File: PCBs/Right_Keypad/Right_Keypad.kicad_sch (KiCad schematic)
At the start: 33 parts, among them J1 Conn_Right_Keypad, SW1 SW_Push, SW10 SW_Push, SW11 SW_Push, SW12 SW_Push, SW13 SW_Push, SW14 SW_Push, SW15 SW_Push, SW16 SW_Push, SW17 SW_Push, SW18 SW_Push, SW19 SW_Push, SW2 SW_Push, SW20 SW_Push, SW21 SW_Push, SW22 SW_Push, SW3 SW_Push, SW4 SW_Push, SW5 SW_Push, SW6 SW_Push, SW7 SW_Push, SW8 SW_Push, SW9 SW_Push, U1 74HC165, U2 74HC165, U3 74HC165

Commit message: wip
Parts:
- C1, C2, C3: footprint (none) -> Capacitor_THT:C_Disc_D5.0mm_W2.5mm_P2.50mm
- J1: footprint (none) -> Connector_IDC:IDC-Header_2x05_P2.54mm_Vertical
- R1: footprint (none) -> Resistor_THT:R_Axial_DIN0207_L6.3mm_D2.5mm_P7.62mm_Horizontal
- SW1, SW10, SW11, SW12, SW13, SW14, SW15, SW16, SW17, SW18, SW19, SW2, SW20, SW21, SW22, SW3, SW4, SW5, SW6, SW7, SW8, SW9: footprint (none) -> Custom_Footprints:SW_PUSH-12mm_Grid
- U1, U2, U3: footprint (none) -> Package_DIP:DIP-16_W7.62mm
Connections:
- net +5V: now also C2.2, C3.2, U2.16 (VCC), U3.16 (VCC)
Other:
- moved on the sheet: C1

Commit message: before moving keypad shift regs
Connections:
- net at RN3.2 (R1): now also U3.3 (D4); no longer U3.6 (D7)
- net at RN3.3 (R2): now also U3.14 (D3); no longer U3.5 (D6)
- net at RN3.4 (R3), U3.4 (D5): now also SW14.2; no longer SW22.2
- net at RN3.9 (R8), U3.11 (D0): now also SW22.2; no longer SW17.2
- net at RN1.3 (R2), SW7.2: now also U1.14 (D3); no longer U1.5 (D6)
- net at SW8.2, U1.6 (D7): now also RN1.8 (R7); no longer RN1.2 (R1)
- net at RN1.9 (R8), U1.11 (D0): now also SW3.2; no longer SW1.2
- net at RN1.4 (R3), U1.4 (D5): now also SW4.2; no longer SW6.2
- net at RN2.9 (R8), U2.11 (D0): now also SW19.2; no longer SW9.2
- net at RN2.4 (R3), U2.4 (D5): now also SW11.2; no longer SW14.2
- new net: RN3.5 (R4), SW15.2, U3.13 (D2)
- new net: RN3.6 (R5), SW16.2, U3.5 (D6)
- new net: RN3.7 (R6), SW20.2, U3.12 (D1)
- new net: RN3.8 (R7), SW21.2, U3.6 (D7)
- new net: RN1.6 (R5), SW2.2, U1.5 (D6)
- new net: RN1.5 (R4), SW1.2, U1.13 (D2)
- new net: RN1.7 (R6), SW5.2, U1.12 (D1)
- new net: RN1.2 (R1), SW10.2, U1.3 (D4)
- new net: RN2.3 (R2), SW6.2, U2.14 (D3)
- new net: RN2.8 (R7), SW18.2, U2.6 (D7)
- new net: RN2.2 (R1), SW9.2, U2.3 (D4)
- new net: RN2.7 (R6), SW17.2, U2.12 (D1)
- new net: RN2.5 (R4), SW12.2, U2.13 (D2)
- new net: RN2.6 (R5), SW13.2, U2.5 (D6)
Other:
- moved on the sheet: SW1, SW10, SW11, SW12, SW13, SW14, SW15, SW16, SW17, SW18, SW19, SW2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

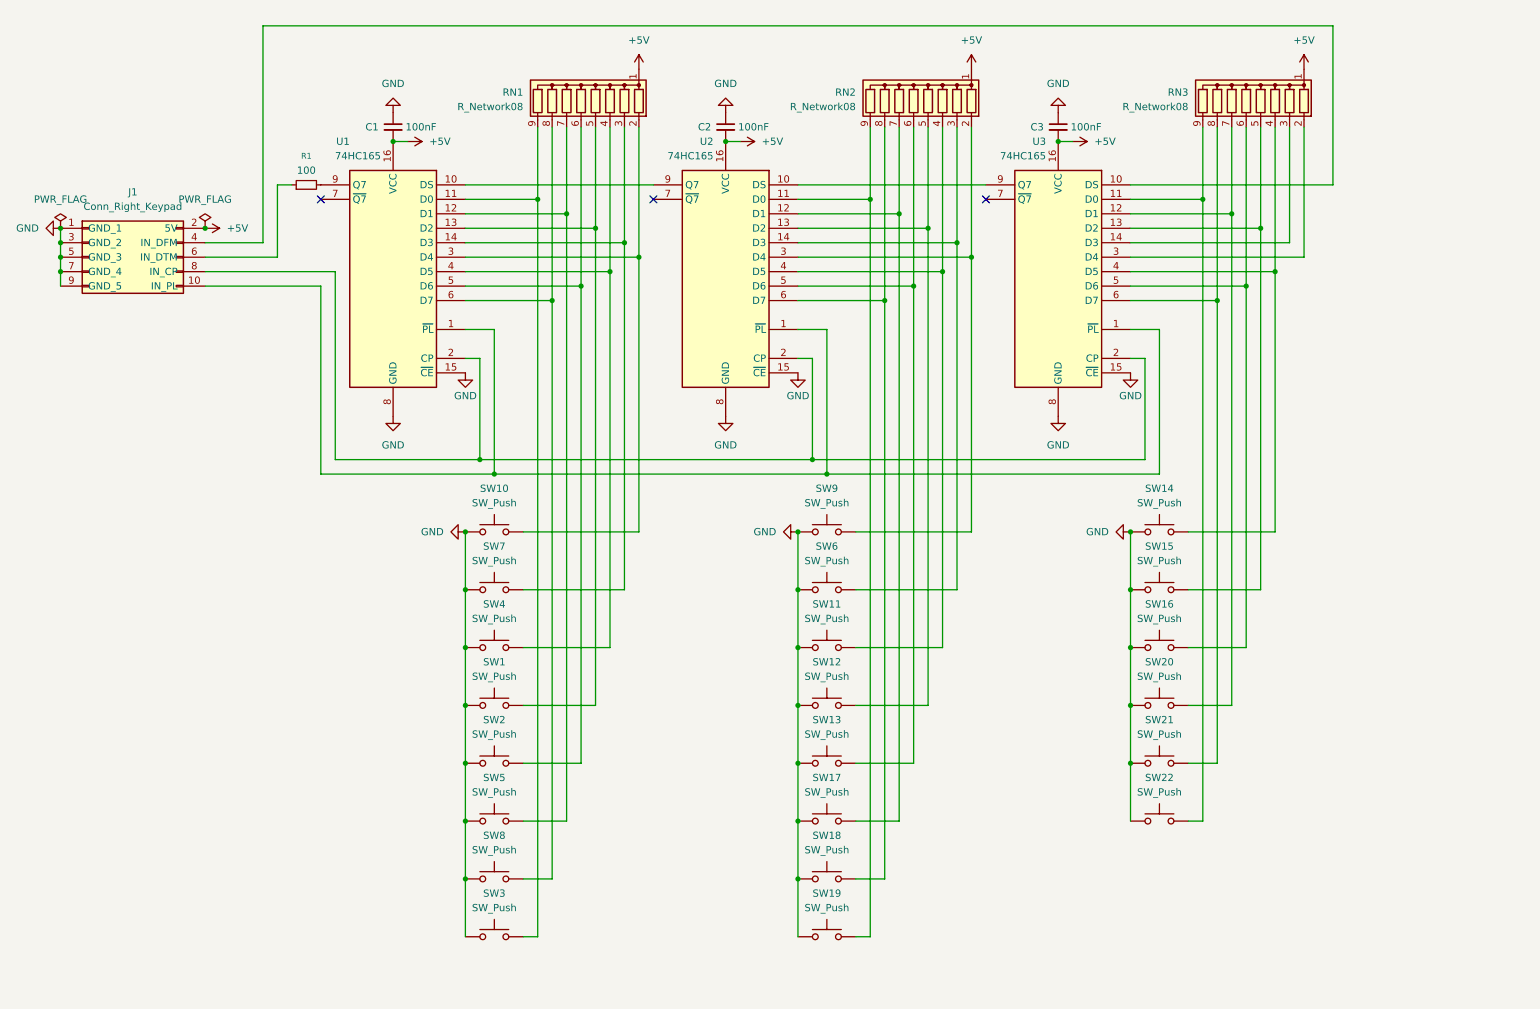
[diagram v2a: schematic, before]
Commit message: Moved shift registers
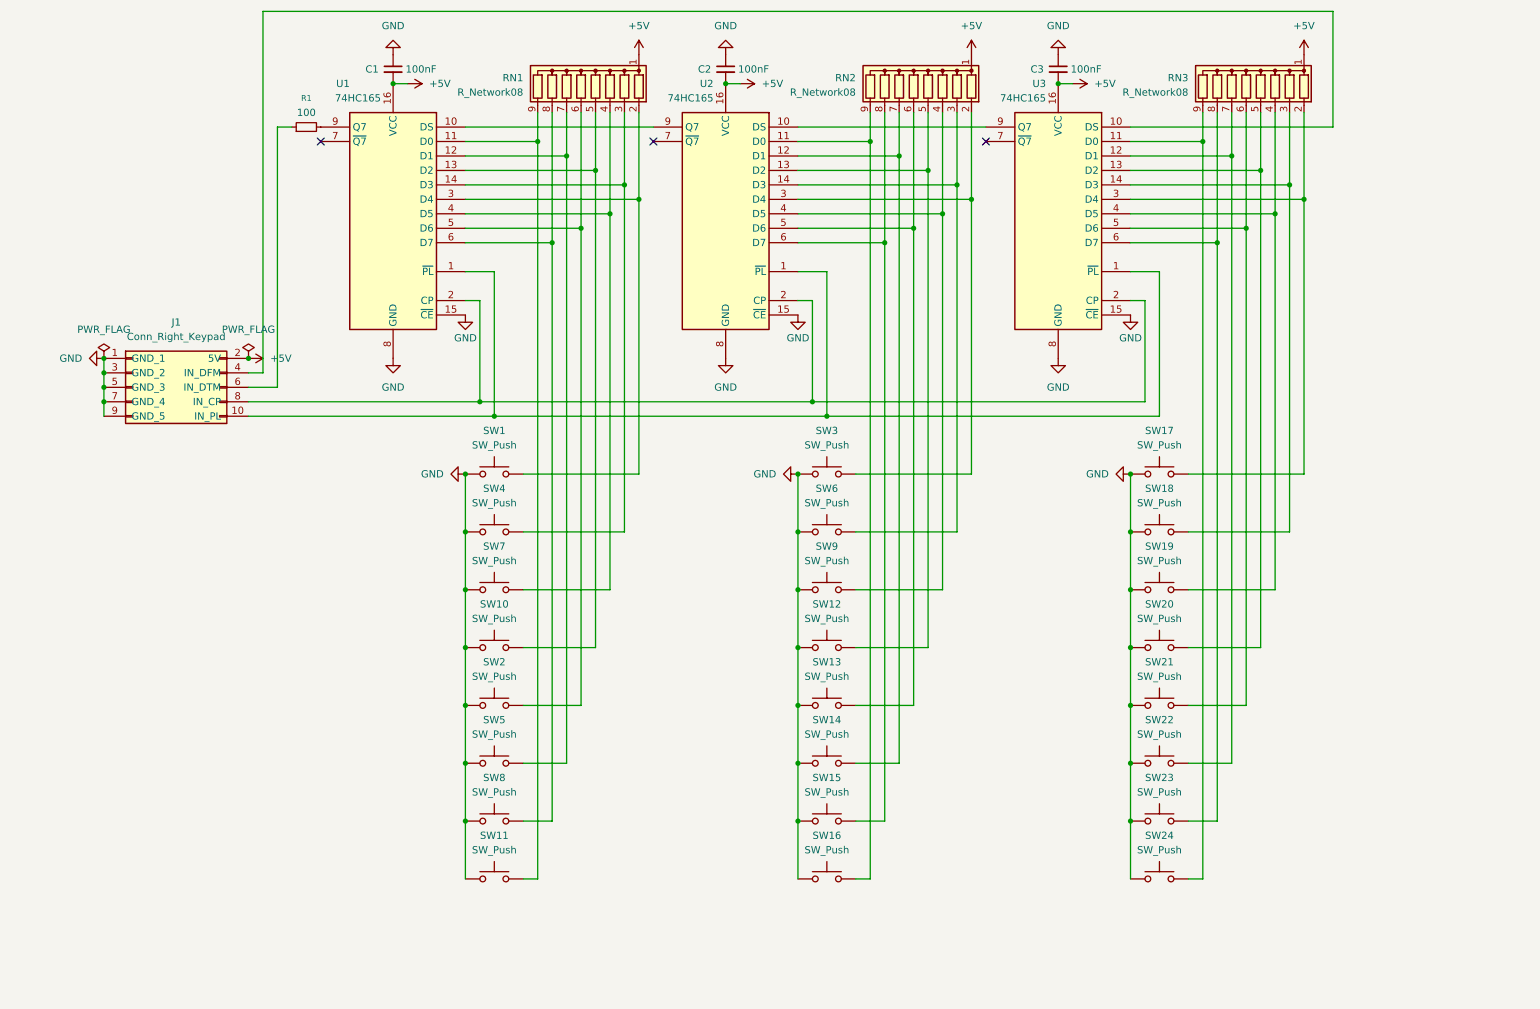
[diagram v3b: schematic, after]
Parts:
- added SW23, SW24: SW_Push, Custom_Footprints:SW_PUSH-12mm_Grid, symbol Switch:SW_Push
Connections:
- net GND: now also SW23.1, SW24.1
- net at RN3.5 (R4), U3.13 (D2): now also SW20.2; no longer SW15.2
- net at RN3.2 (R1), U3.3 (D4): now also SW17.2
- net at RN3.3 (R2), U3.14 (D3): now also SW18.2
- net at RN3.4 (R3), U3.4 (D5): now also SW19.2; no longer SW14.2
- net at RN3.6 (R5), U3.5 (D6): now also SW21.2; no longer SW16.2
- net at RN3.7 (R6), U3.12 (D1): now also SW22.2; no longer SW20.2
- net at RN3.8 (R7), U3.6 (D7): now also SW23.2; no longer SW21.2
- net at RN3.9 (R8), U3.11 (D0): now also SW24.2; no longer SW22.2
- net at RN2.4 (R3), U2.4 (D5): now also SW9.2; no longer SW11.2
- net at RN1.3 (R2), U1.14 (D3): now also SW4.2; no longer SW7.2
- net at RN1.9 (R8), U1.11 (D0): now also SW11.2; no longer SW3.2
- net at RN1.4 (R3), U1.4 (D5): now also SW7.2; no longer SW4.2
- net at RN1.5 (R4), U1.13 (D2): now also SW10.2; no longer SW1.2
- net at RN1.2 (R1), U1.3 (D4): now also SW1.2; no longer SW10.2
- net at RN2.8 (R7), U2.6 (D7): now also SW15.2; no longer SW18.2
- net at RN2.2 (R1), U2.3 (D4): now also SW3.2; no longer SW9.2
- net at RN2.7 (R6), U2.12 (D1): now also SW14.2; no longer SW17.2
- net at RN2.9 (R8), U2.11 (D0): now also SW16.2; no longer SW19.2
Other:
- moved on the sheet: C1, C2, C3, J1, R1, RN1, RN2, RN3, SW1, SW10, SW11, SW12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

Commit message: before UART+RS485
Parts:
- removed C2, C3: 100nF, Capacitor_THT:C_Disc_D5.0mm_W2.5mm_P2.50mm, symbol Device:C_Small
- removed RN2, RN3: R_Network08, Resistor_THT:R_Array_SIP9, symbol Device:R_Network08
- removed U2, U3: 74HC165, Package_DIP:DIP-16_W7.62mm, symbol 74xx:74HC165
- added D1, D10, D11, D12, D13, D14, D15, D16, D17, D18, D19, D2, D20, D21, D22, D23, D24, D3, D4, D5, D6, D7, D8, D9: D, Diode_SMD:D_SOD-123, symbol Device:D
- added Q1, Q2, Q3: NPN, Package_TO_SOT_THT:TO-92_Inline, symbol Simulation_SPICE:NPN
- added R2, R3, R4: 10k, Resistor_THT:R_Axial_DIN0207_L6.3mm_D2.5mm_P7.62mm_Horizontal, symbol Device:R_Small
- J1: footprint Connector_IDC:IDC-Header_2x05_P2.54mm_Vertical -> Connector_IDC:IDC-Header_2x08_P2.54mm_Vertical
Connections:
- net GND: now also J1.11 (GND_6), J1.13 (GND_7), J1.15 (GND_8), Q1.3 (E), Q2.3 (E), Q3.3 (E); no longer SW1.1, SW10.1, SW11.1, SW12.1, SW13.1, SW14.1, SW15.1, SW16.1, SW17.1, SW18.1, SW19.1, SW2.1, SW20.1, SW21.1, SW22.1, SW23.1, SW24.1, SW3.1, SW4.1, SW5.1, SW6.1, SW7.1, SW8.1, SW9.1
- net at SW15.2: now also D15.1 (K)
- net at SW17.2: now also D17.1 (K)
- net at SW18.2: now also D18.1 (K)
- net at SW19.2: now also D19.1 (K)
- net at SW20.2: now also D20.1 (K)
- net at SW21.2: now also D21.1 (K)
- net at SW22.2: now also D22.1 (K)
- net at SW23.2: now also D23.1 (K)
- net at SW24.2: now also D24.1 (K)
- net at RN1.9 (R8), U1.11 (D0): now also D1.2 (A), D17.2 (A), D9.2 (A); no longer SW11.2
- net at RN1.4 (R3), U1.4 (D5): now also D14.2 (A), D22.2 (A), D6.2 (A); no longer SW7.2
- net at SW3.2: now also D3.1 (K)
- net at J1.4 (IN_DFM): now also U1.10 (DS)
- net at SW6.2: now also D6.1 (K)
- net at SW16.2: now also D16.1 (K)
- net at SW9.2: now also D9.1 (K)
- net at SW12.2: now also D12.1 (K)
- net at SW13.2: now also D13.1 (K)
- net at SW14.2: now also D14.1 (K)
- new net: Q2.1 (C), SW10.1, SW11.1, SW12.1, SW13.1, SW14.1, SW15.1, SW16.1, SW9.1
- new net: D10.1 (K), SW10.2
- new net: D13.2 (A), D21.2 (A), D5.2 (A), RN1.5 (R4), U1.3 (D4)
- new net: D12.2 (A), D20.2 (A), D4.2 (A), RN1.6 (R5), U1.14 (D3)
- new net: Q1.1 (C), SW1.1, SW2.1, SW3.1, SW4.1, SW5.1, SW6.1, SW7.1, SW8.1
- new net: D2.1 (K), SW2.2
- new net: D4.1 (K), SW4.2
- new net: D1.1 (K), SW1.2
- new net: D11.2 (A), D19.2 (A), D3.2 (A), RN1.7 (R6), U1.13 (D2)
- new net: Q2.2 (B), R3.2
- new net: Q3.1 (C), SW17.1, SW18.1, SW19.1, SW20.1, SW21.1, SW22.1, SW23.1, SW24.1
- new net: D5.1 (K), SW5.2
- new net: D7.1 (K), SW7.2
- new net: D16.2 (A), D24.2 (A), D8.2 (A), RN1.2 (R1), U1.6 (D7)
- new net: J1.16 (ROW_3), R4.1
- new net: Q3.2 (B), R4.2
- new net: D15.2 (A), D23.2 (A), D7.2 (A), RN1.3 (R2), U1.5 (D6)
- new net: D10.2 (A), D18.2 (A), D2.2 (A), RN1.8 (R7), U1.12 (D1)
- new net: J1.14 (ROW_2), R3.1
- new net: D8.1 (K), SW8.2
- new net: D11.1 (K), SW11.2
- new net: Q1.2 (B), R2.2
- new net: J1.12 (ROW_1), R2.1
- no-connect marks 3 -> 1
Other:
- moved on the sheet: C1, R1, RN1, U1

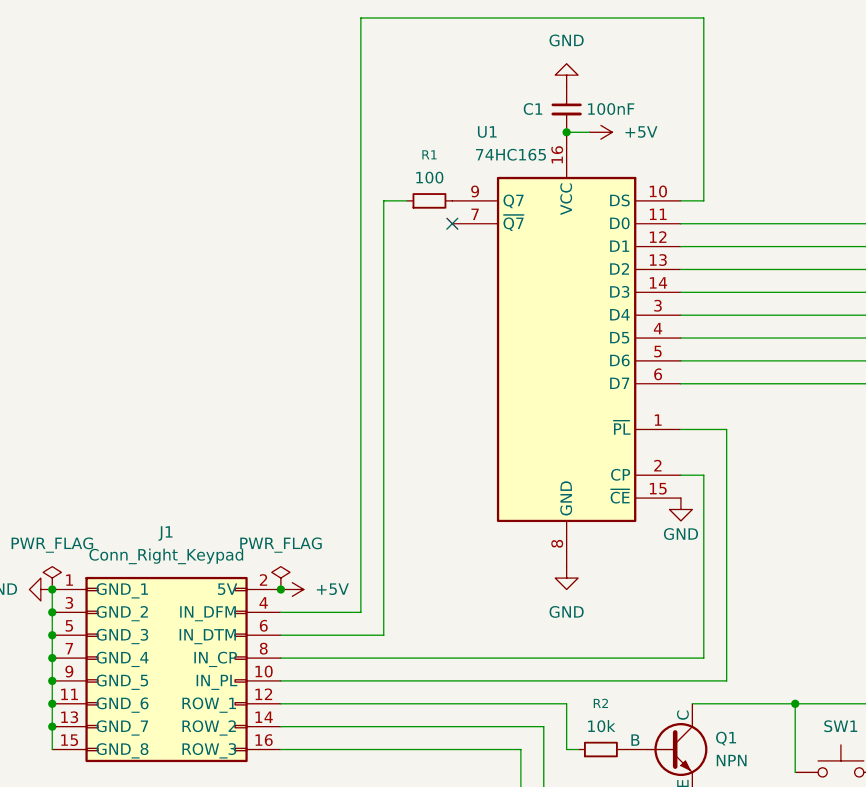
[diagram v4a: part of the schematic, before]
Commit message: UART+RS485 + KiCad 10 + keypad PCB v1
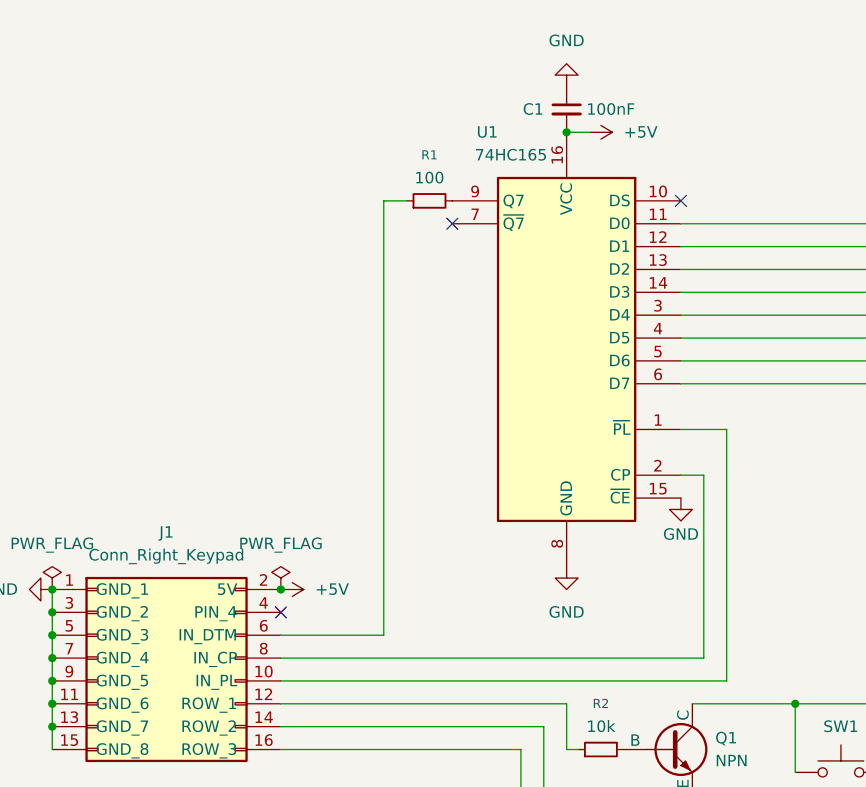
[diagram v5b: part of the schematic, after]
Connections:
- net at U1.10 (DS): no longer J1.4 (IN_DFM)
- no-connect marks 1 -> 3

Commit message: ESD protection and stuff
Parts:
- added H1, H2, H3, H4: MountingHole_Pad, MountingHole:MountingHole_3.2mm_M3_Pad_TopBottom, symbol Mechanical:MountingHole_Pad
- Q1, Q2, Q3: symbol Simulation_SPICE:NPN -> Transistor_BJT:Q_NPN_CBE
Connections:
- net at D12.2 (A), D20.2 (A), D4.2 (A)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: now also U1.11 (D0); no longer U1.14 (D3)
- net at D11.2 (A), D19.2 (A), D3.2 (A)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: now also U1.12 (D1); no longer U1.13 (D2)
- net at D10.2 (A), D18.2 (A), D2.2 (A)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: now also U1.13 (D2); no longer U1.12 (D1)
- net at D1.2 (A), D17.2 (A), D9.2 (A)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: now also U1.14 (D3); no longer U1.11 (D0)
- new net Chassis: H1.1, H2.1, H3.1, H4.1

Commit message: finishing touches and silkscreen stuff
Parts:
- H1, H2, H3, H4: footprint MountingHole:MountingHole_3.2mm_M3_Pad_TopBottom -> MountingHole:MountingHole_3.2mm_M3_Pad
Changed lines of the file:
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@@
 	)
 	(junction
+		(at 22.86 151.13)
+		(diameter 0)
+		(color 0 0 0 0)
+	)
+	(junction
 		(at 255.27 68.58)
 		(diameter 0)
@@
 	(wire
 		(pts
+			(xy 22.86 152.4) (xy 22.86 151.13)
+		)
+		(stroke
+			(width 0)
+			(type default)
+		)
+	)
+	(wire
+		(pts
 			(xy 180.34 139.7) (xy 180.34 147.32)
 		)
@@
 			)
 		)
-		(property "Footprint" "MountingHole:MountingHole_3.2mm_M3_Pad_TopBottom"
+		(property "Footprint" "MountingHole:MountingHole_3.2mm_M3_Pad"
 			(at 25.4 132.08 0)
 			(hide yes)
@@
 	)
 	(symbol
+		(lib_id "power:PWR_FLAG")
+		(at 22.86 151.13 270)
+		(unit 1)
+		(body_style 1)
+		(exclude_from_sim no)
+		(in_bom yes)
+		(on_board yes)
+		(in_pos_files yes)
+		(dnp no)
+		(fields_autoplaced yes)
+		(property "Reference" "#FLG03"
+			(at 24.765 151.13 0)
+			(hide yes)
+			(show_name no)
+			(do_not_autoplace no)
+			(effects
+				(font
+					(size 1.27 1.27)
+				)
+			)
+		)
+		(property "Value" "PWR_FLAG"
+			(at 26.67 151.1299 90)
+			(show_name no)
+			(do_not_autoplace no)
+			(effects
+				(font
+					(size 1.27 1.27)
+				)
+				(justify left)
+			)
+		)
+		(property "Footprint" ""
+			(at 22.86 151.13 0)
+			(hide yes)
+			(show_name no)
+			(do_not_autoplace no)
+			(effects
+				(font
+					(size 1.27 1.27)
+				)
+			)
+		)
+		(property "Datasheet" ""
+			(at 22.86 151.13 0)
+			(hide yes)
+			(show_name no)
+			(do_not_autoplace no)
+			(effects
+				(font
+					(size 1.27 1.27)
+				)
+			)
+		)
+		(property "Description" "Special symbol for telling ERC where power comes from"
+			(at 22.86 151.13 0)
+			(hide yes)
+			(show_name no)
+			(do_not_autoplace no)
+			(effects
+				(font
+					(size 1.27 1.27)
+				)
+			)
+		)
+		(pin "1"
+		)
+		(instances
+			(project "Right_Keypad"
+				(path "/ba685c3e-917d-4c11-a4ac-87b5dc0bd447"
+					(reference "#FLG03")
+					(unit 1)
+				)
+			)
+		)
+	)
+	(symbol
 		(lib_id "Switch:SW_Push")
 		(at 109.22 111.76 0)
@@
 			)
 		)
-		(property "Footprint" "MountingHole:MountingHole_3.2mm_M3_Pad_TopBottom"
+		(property "Footprint" "MountingHole:MountingHole_3.2mm_M3_Pad"
 			(at 25.4 137.16 0)
 			(hide yes)
@@
 			)
 		)
-		(property "Footprint" "MountingHole:MountingHole_3.2mm_M3_Pad_TopBottom"
+		(property "Footprint" "MountingHole:MountingHole_3.2mm_M3_Pad"
 			(at 25.4 147.32 0)
 			(hide yes)
@@
 			)
 		)
-		(property "Footprint" "MountingHole:MountingHole_3.2mm_M3_Pad_TopBottom"
+		(property "Footprint" "MountingHole:MountingHole_3.2mm_M3_Pad"
 			(at 25.4 142.24 0)
 			(hide yes)
@@
 	(symbol
 		(lib_id "power:Earth")
-		(at 22.86 151.13 0)
+		(at 22.86 152.4 0)
 		(unit 1)
 		(body_style 1)
@@
 		(fields_autoplaced yes)
 		(property "Reference" "#PWR06"
-			(at 22.86 157.48 0)
+			(at 22.86 158.75 0)
 			(hide yes)
 			(show_name no)
@@
 		)
 		(property "Value" "Chassis"
-			(at 22.86 156.21 0)
+			(at 22.86 157.48 0)
 			(show_name no)
 			(do_not_autoplace no)
@@
 		)
 		(property "Footprint" ""
-			(at 22.86 151.13 0)
+			(at 22.86 152.4 0)
 			(hide yes)
 			(show_name no)
@@
 		)
 		(property "Datasheet" ""
-			(at 22.86 151.13 0)
+			(at 22.86 152.4 0)
 			(hide yes)
 			(show_name no)
@@
 		)
 		(property "Description" "Power symbol creates a global label with name \"Earth\""
-			(at 22.86 151.13 0)
+			(at 22.86 152.4 0)
 			(hide yes)
 			(show_name no)
